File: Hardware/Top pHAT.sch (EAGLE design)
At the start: 66 parts, among them J1 QWIIC, J2 AVR_SPI_PROG_3X2TESTPOINTS, J3 2.4" TFT, Q2 1.1A/60V/600mΩ, U1 RASPBERRY_PI_40BTM-NOHOLES, U2 ADMP401, U3 ADMP401, U4 WM8960, U5 ATTINY84, Y1 24 MHz

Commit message: post checklist changes
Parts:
- S6: value (none) -> Joystick
- U1: value RASPBERRY_PI_40BTM-NOHOLES -> Raspberry Pi Header
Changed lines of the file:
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@@
 </classes>
 <parts>
-<part name="U1" library="SparkFun-Connectors" deviceset="RASPBERRY_PI_40" device="BTM-NOHOLES" value=""/>
+<part name="U1" library="SparkFun-Connectors" deviceset="RASPBERRY_PI_40" device="BTM-NOHOLES" value="Raspberry Pi Header"/>
 <part name="S3" library="SparkFun-Switches" deviceset="MOMENTARY-SWITCH-SPST" device="-SMD-5.2MM-TALL"/>
 <part name="S4" library="SparkFun-Switches" deviceset="MOMENTARY-SWITCH-SPST" device="-SMD-5.2MM-TALL"/>
 <part name="U2" library="SparkFun-Sensors" deviceset="ADMP401" device=""/>
 <part name="U3" library="SparkFun-Sensors" deviceset="ADMP401" device=""/>
-<part name="S6" library="SparkFun-Switches" deviceset="JOYSTICK_MINI" device=""/>
+<part name="S6" library="SparkFun-Switches" deviceset="JOYSTICK_MINI" device="" value="Joystick"/>
 <part name="H1" library="SparkFun-Hardware" deviceset="STAND-OFF" device="TIGHT"/>
 <part name="H2" library="SparkFun-Hardware" deviceset="STAND-OFF" device="TIGHT"/>

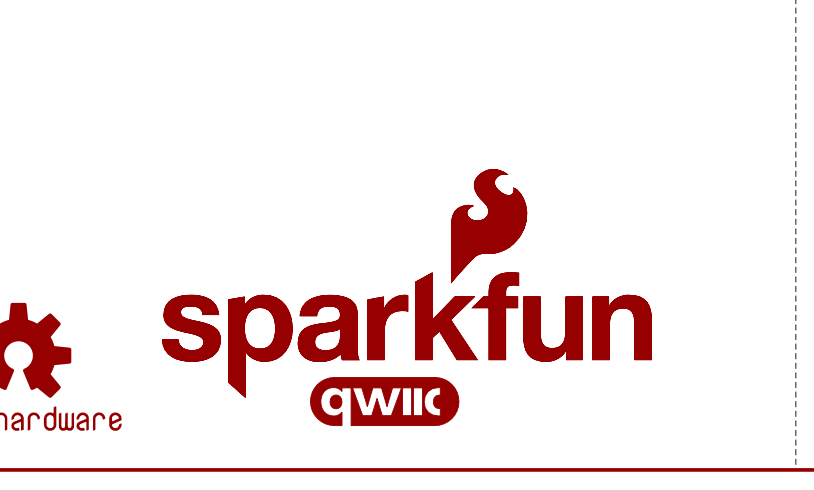
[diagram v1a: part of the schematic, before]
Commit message: adding top pHAT silk
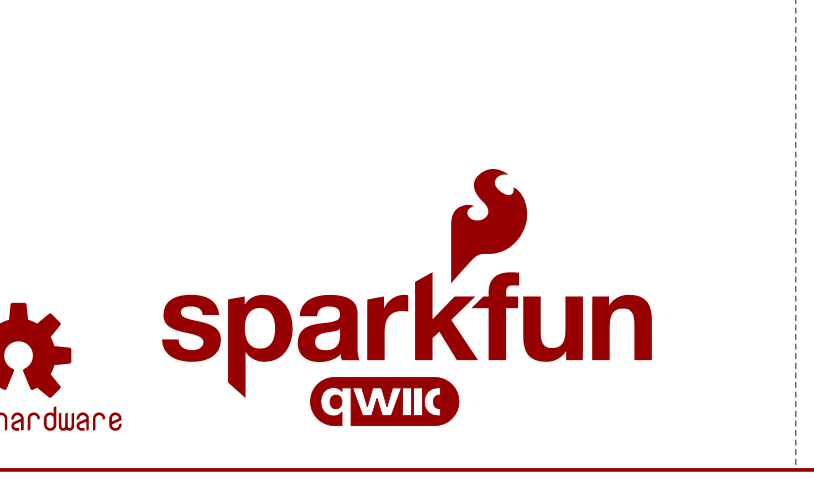
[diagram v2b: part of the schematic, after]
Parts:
- removed LOGO1: SFE_LOGO_NAME_FLAME.1_INCH, SparkFun-Aesthetics:SFE_LOGO_NAME_FLAME.1_INCH
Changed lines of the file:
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@@
 <part name="SUPPLY11" library="SparkFun-PowerSymbols" deviceset="3.3V" device=""/>
 <part name="GND9" library="SparkFun-PowerSymbols" deviceset="GND" device=""/>
-<part name="LOGO1" library="SparkFun-Aesthetics" deviceset="SFE_LOGO_NAME_FLAME" device=".1_INCH"/>
 <part name="LOGO2" library="SparkFun-Aesthetics" deviceset="SFE_LOGO_NAME_FLAME" device=".4_INCH"/>
 <part name="LOGO3" library="SparkFun-Aesthetics" deviceset="QWIIC_LOGO" device="_4MM"/>
@@
 <attribute name="VALUE" x="205.74" y="136.906" size="1.778" layer="96" rot="MR0" align="top-center"/>
 </instance>
-<instance part="LOGO1" gate="G$1" x="205.74" y="7.62" smashed="yes"/>
 <instance part="LOGO2" gate="G$1" x="205.74" y="7.62" smashed="yes"/>
 <instance part="LOGO3" gate="G$1" x="231.14" y="7.62" smashed="yes"/>

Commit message: v11 - mic and vector buzzards/graphics
-swapped out the mic for the ICS-40180
-updated labels to new vector buzzards
-converted top phat logo into vector version, currently in mini library.
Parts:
- removed U2, U3: ADMP401, SparkFun-Sensors:ADMP401
- added U6, U7: ICS40180, ICS-40180:ICS40180
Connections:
- net GND: now also U6.GND, U7.GND; no longer U2.GND@2, U2.GND@4, U2.GND@6, U3.GND@2, U3.GND@4, U3.GND@6
- net LEFTMIC: now also U6.OUT; no longer U2.OUT
- net MICBIAS: now also U6.VDD, U7.VDD; no longer U2.VDD, U3.VDD
- net RIGHTMIC: now also U7.OUT; no longer U3.OUT
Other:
- note added: "Revised by: Pete Lewis"
- note added: "v11"
- note removed: "v10"
- moved on the sheet: C10, C11

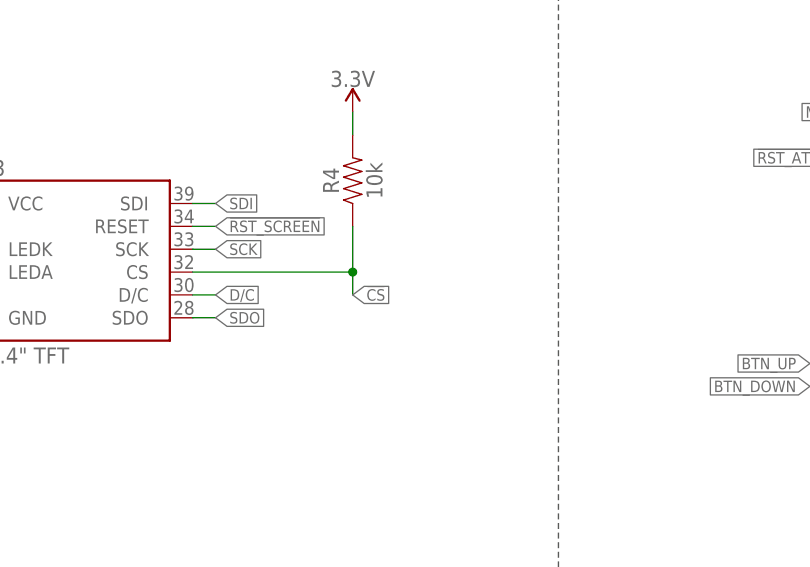
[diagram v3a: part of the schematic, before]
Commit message: first run of checklist stuff
-CS net in schematic needed a nudge.
-enlarged top phat logo polygon lines to 0.0005"
-Added link to Qwiic Button repo in readme - for firmware and fusebits, if needed by user.
-added mic datasheet for good measure.
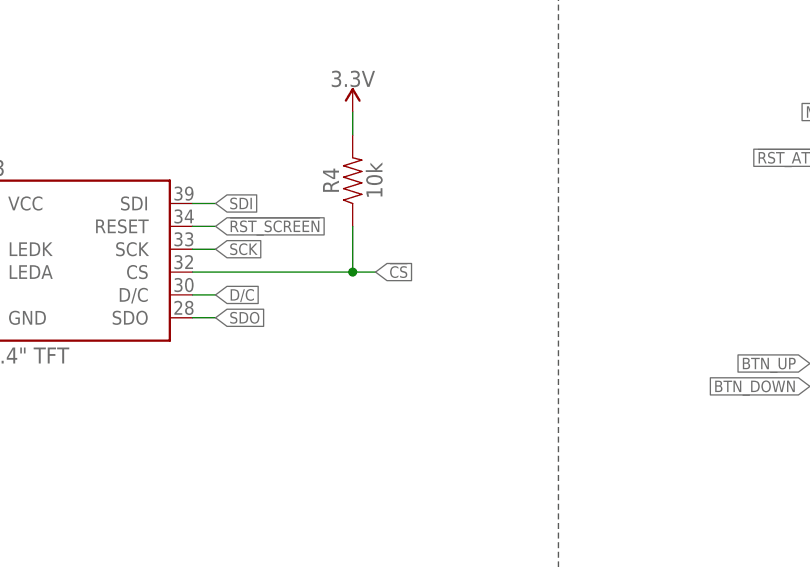
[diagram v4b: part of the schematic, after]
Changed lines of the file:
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@@
 <pinref part="J3" gate="G$1" pin="CS"/>
 <wire x1="236.22" y1="147.32" x2="254" y2="147.32" width="0.1524" layer="91"/>
-<label x="254" y="144.78" size="1.27" layer="95" xref="yes"/>
+<label x="256.54" y="147.32" size="1.27" layer="95" xref="yes"/>
 <pinref part="R4" gate="G$1" pin="1"/>
-<wire x1="254" y1="147.32" x2="254" y2="144.78" width="0.1524" layer="91"/>
+<wire x1="254" y1="147.32" x2="256.54" y2="147.32" width="0.1524" layer="91"/>
 <wire x1="254" y1="152.4" x2="254" y2="147.32" width="0.1524" layer="91"/>
 <junction x="254" y="147.32"/>
